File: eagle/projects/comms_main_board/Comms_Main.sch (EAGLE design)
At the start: 96 parts, among them J1 RECE-20279-001E, J2 PRT-12639, J3 PRT-12639, J4 PRT-12639, J5 PRT-12639, J6 MOL-KK-3P-RA, J7 MOL-KK-5P-V, J8 RECEPTACLE-2x20-254MM, Q1 CSD17579Q3A, U1 TPS562209DDCT, U11 TPS562209DDCT, U2 LP2985-33DBVR, U3 LP5900TLX-3.3/NOPB, U4 TPS562209DDCT, U5 LMZ34002RKGR, U6 LM3488MMX/NOPB, U7 PCT2075D,118, U8 MS560702BA03-50, U9 MAX-M8Q

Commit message: PTT Switch, ATV POT Connector
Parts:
- added J9: MOL-KK-3P-RA, daqcs:MOLKK_3PIN_3RA_RA
- added R36: 0.0, comms:RES_0R0_0805
- added R37: 1k, comms:RES_1R0_0603
- added U12: (no value), comms:MMBT3904-7-F
- J1: value RECE-20279-001E -> (none); device comms:IPEX-20279-001E -> comms:SMA_EDGE
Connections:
- new net N$52: R36.1, U12.E
- new net N$53: R37.2, U12.B
- new net POT_A: J9.1
- new net POT_B: J9.2
- new net POT_W: J9.3
- new net PTT_GPIO: R37.1
- net GND: now also J1.GND@0, J1.GND@2, J1.GND@3, R36.2
- net N$24: now also J1.SIGNAL; no longer J1.1
- net PTT: now also U12.C
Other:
- note added: "ATV POT Connector"
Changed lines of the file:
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@@
 <part name="FRAME4" library="frames" deviceset="A4L-LOC" device=""/>
 <part name="SUPPLY6" library="supply2" deviceset="GND" device=""/>
-<part name="J1" library="comms" deviceset="IPEX-20279-001E" device="" value="RECE-20279-001E"/>
 <part name="R16" library="comms" deviceset="RES" device="_0603" technology="_0R10" value="10"/>
 <part name="C22" library="comms" deviceset="CAP" device="_0805" technology="_10NF0" value="10nF"/>
@@
 <part name="J8" library="comms" deviceset="RECEPTACLE-2X20-254MM" device="" value="RECEPTACLE-2x20-254MM"/>
 <part name="SUPPLY16" library="supply2" deviceset="GND" device=""/>
+<part name="J1" library="comms" deviceset="SMA_EDGE" device=""/>
+<part name="R36" library="comms" deviceset="RES" device="_0805" technology="_0R0" value="0.0"/>
+<part name="SUPPLY17" library="supply2" deviceset="GND" device=""/>
+<part name="U12" library="comms" deviceset="MMBT3904-7-F" device=""/>
+<part name="R37" library="comms" deviceset="RES" device="_0603" technology="_1R0" value="1k"/>
+<part name="J9" library="daqcs" deviceset="MOLKK_3PIN" device="_RA" technology="_3RA" value="MOL-KK-3P-RA"/>
 </parts>
 <sheets>
@@
 <instance part="FRAME4" gate="G$1" x="0" y="0"/>
 <instance part="SUPPLY6" gate="GND" x="109.22" y="68.58"/>
-<instance part="J1" gate="G$1" x="55.88" y="116.84"/>
 <instance part="R16" gate="G$1" x="93.98" y="101.6"/>
 <instance part="C22" gate="G$1" x="76.2" y="78.74"/>
@@
 <instance part="R39" gate="G$1" x="167.64" y="101.6"/>
 <instance part="U9" gate="G$1" x="134.62" y="106.68"/>
+<instance part="J1" gate="1" x="53.34" y="116.84"/>
 </instances>
 <busses>
@@
 <segment>
 <pinref part="SUPPLY6" gate="GND" pin="GND"/>
-<wire x1="109.22" y1="121.92" x2="109.22" y2="114.3" width="0.1524" layer="91"/>
-<wire x1="109.22" y1="114.3" x2="109.22" y2="111.76" width="0.1524" layer="91"/>
+<wire x1="109.22" y1="121.92" x2="109.22" y2="111.76" width="0.1524" layer="91"/>
 <wire x1="109.22" y1="111.76" x2="109.22" y2="76.2" width="0.1524" layer="91"/>
 <wire x1="109.22" y1="76.2" x2="109.22" y2="73.66" width="0.1524" layer="91"/>
@@
 <junction x="109.22" y="73.66"/>
 <wire x1="111.76" y1="121.92" x2="109.22" y2="121.92" width="0.1524" layer="91"/>
-<pinref part="J1" gate="G$1" pin="GND@1"/>
-<wire x1="58.42" y1="114.3" x2="109.22" y2="114.3" width="0.1524" layer="91"/>
-<junction x="109.22" y="114.3"/>
 <pinref part="C22" gate="G$1" pin="2"/>
 <wire x1="76.2" y1="76.2" x2="109.22" y2="76.2" width="0.1524" layer="91"/>
@@
 <pinref part="U9" gate="G$1" pin="10_GND"/>
 <pinref part="U9" gate="G$1" pin="12_GND"/>
+<pinref part="J1" gate="1" pin="GND@0"/>
+<wire x1="50.8" y1="111.76" x2="48.26" y2="111.76" width="0.1524" layer="91"/>
+<wire x1="48.26" y1="111.76" x2="48.26" y2="109.22" width="0.1524" layer="91"/>
+<wire x1="48.26" y1="109.22" x2="48.26" y2="106.68" width="0.1524" layer="91"/>
+<wire x1="48.26" y1="106.68" x2="48.26" y2="104.14" width="0.1524" layer="91"/>
+<wire x1="48.26" y1="104.14" x2="48.26" y2="76.2" width="0.1524" layer="91"/>
+<wire x1="48.26" y1="76.2" x2="76.2" y2="76.2" width="0.1524" layer="91"/>
+<junction x="76.2" y="76.2"/>
+<pinref part="J1" gate="1" pin="GND@1"/>
+<wire x1="50.8" y1="109.22" x2="48.26" y2="109.22" width="0.1524" layer="91"/>
+<junction x="48.26" y="109.22"/>
+<pinref part="J1" gate="1" pin="GND@2"/>
+<wire x1="50.8" y1="106.68" x2="48.26" y2="106.68" width="0.1524" layer="91"/>
+<junction x="48.26" y="106.68"/>
+<pinref part="J1" gate="1" pin="GND@3"/>
+<wire x1="50.8" y1="104.14" x2="48.26" y2="104.14" width="0.1524" layer="91"/>
+<junction x="48.26" y="104.14"/>
 </segment>
 </net>
 <net name="N$24" class="0">
 <segment>
-<pinref part="J1" gate="G$1" pin="1"/>
 <wire x1="58.42" y1="116.84" x2="76.2" y2="116.84" width="0.1524" layer="91"/>
 <pinref part="L5" gate="G$1" pin="1"/>
@@
 <junction x="76.2" y="116.84"/>
 <pinref part="U9" gate="G$1" pin="11_RF_IN"/>
+<pinref part="J1" gate="1" pin="SIGNAL"/>
 </segment>
 </net>
@@
 <instance part="J4" gate="G$1" x="55.88" y="66.04"/>
 <instance part="J5" gate="G$1" x="55.88" y="40.64"/>
+<instance part="R36" gate="G$1" x="180.34" y="76.2" rot="R270"/>
+<instance part="SUPPLY17" gate="GND" x="180.34" y="66.04"/>
+<instance part="U12" gate="A" x="180.34" y="93.98"/>
+<instance part="R37" gate="G$1" x="157.48" y="93.98"/>
 </instances>
 <busses>
@@
 <pinref part="J2" gate="G$1" pin="EARTH"/>
 </segment>
+<segment>
+<pinref part="SUPPLY17" gate="GND" pin="GND"/>
+<pinref part="R36" gate="G$1" pin="2"/>
+<wire x1="180.34" y1="68.58" x2="180.34" y2="71.12" width="0.1524" layer="91"/>
+</segment>
 </net>
 <net name="N$32" class="0">
@@
 <segment>
 <pinref part="R27" gate="G$1" pin="1"/>
-<wire x1="132.08" y1="109.22" x2="167.64" y2="109.22" width="0.1524" layer="91"/>
+<wire x1="132.08" y1="109.22" x2="180.34" y2="109.22" width="0.1524" layer="91"/>
 <label x="154.94" y="109.22" size="1.778" layer="95"/>
+<wire x1="180.34" y1="109.22" x2="180.34" y2="104.14" width="0.1524" layer="91"/>
+<pinref part="U12" gate="A" pin="C"/>
+</segment>
+</net>
+<net name="N$52" class="0">
+<segment>
+<pinref part="R36" gate="G$1" pin="1"/>
+<wire x1="180.34" y1="81.28" x2="180.34" y2="86.36" width="0.1524" layer="91"/>
+<pinref part="U12" gate="A" pin="E"/>
+<wire x1="180.34" y1="81.28" x2="180.34" y2="83.82" width="0.1524" layer="91"/>
+</segment>
+</net>
+<net name="N$53" class="0">
+<segment>
+<pinref part="U12" gate="A" pin="B"/>
+<pinref part="R37" gate="G$1" pin="2"/>
+<wire x1="172.72" y1="93.98" x2="162.56" y2="93.98" width="0.1524" layer="91"/>
+</segment>
+</net>
+<net name="PTT_GPIO" class="0">
+<segment>
+<pinref part="R37" gate="G$1" pin="1"/>
+<wire x1="152.4" y1="93.98" x2="132.08" y2="93.98" width="0.1524" layer="91"/>
+<label x="134.62" y="93.98" size="1.778" layer="95"/>
 </segment>
 </net>
@@
 <text x="-73.66" y="38.1" size="1.778" layer="91">DAQCS SPI Connector</text>
 <text x="66.04" y="-45.72" size="1.778" layer="91">Pi Zero Connector</text>
+<text x="-110.49" y="6.35" size="1.778" layer="91">ATV POT Connector</text>
 </plain>
 <instances>
@@
 <instance part="J8" gate="G$1" x="76.2" y="12.7"/>
 <instance part="SUPPLY16" gate="GND" x="76.2" y="-55.88"/>
+<instance part="J9" gate="G$1" x="-106.68" y="22.86"/>
 </instances>
 <busses>
@@
 </segment>
 </net>
+<net name="POT_A" class="0">
+<segment>
+<pinref part="J9" gate="G$1" pin="1"/>
+<wire x1="-93.98" y1="27.94" x2="-81.28" y2="27.94" width="0.1524" layer="91"/>
+<label x="-91.44" y="27.94" size="1.778" layer="95"/>
+</segment>
+</net>
+<net name="POT_B" class="0">
+<segment>
+<pinref part="J9" gate="G$1" pin="2"/>
+<wire x1="-93.98" y1="22.86" x2="-81.28" y2="22.86" width="0.1524" layer="91"/>
+<label x="-91.44" y="22.86" size="1.778" layer="95"/>
+</segment>
+</net>
+<net name="POT_W" class="0">
+<segment>
+<pinref part="J9" gate="G$1" pin="3"/>
+<wire x1="-93.98" y1="17.78" x2="-81.28" y2="17.78" width="0.1524" layer="91"/>
+<label x="-91.44" y="17.78" size="1.778" layer="95"/>
+</segment>
+</net>

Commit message: Did schematic for RS232 level converter. Started work for analog video mux
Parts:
- added C30, C31, C32, C33, C34: 100nF, comms:CAP_100NF0_0805
- added J10: MOL-KK-2-RA, daqcs:MOLKK_2PIN_2RA_2RA
- added J11, J12, J13, J14: MOL-KK-3P-RA, daqcs:MOLKK_3PIN_3RA_RA
- added U13: (no value), comms:MAX232SOIC16
- added U14: MAX4311, comms:MAX4311EEE
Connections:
- new net N$54: C30.1, U13.C1+
- new net N$55: C30.2, U13.C1-
- new net N$56: C31.1, U13.C2+
- new net N$57: C31.2, U13.C2-
- new net OSD_DATA: U13.T1OUT
- new net UART_TXD: U13.T1IN
- new net VID_IN2: U14.IN2
- new net VID_IN3: U14.IN3
- net 3P3V_RS232: now also C32.1, U13.VCC
- net 5V_BOARD: now also C34.1, U13.V+
- net GND: now also C32.2, C33.2, C34.2, U13.GND
- net NEG_5V_BOARD: now also C33.1, U13.V-
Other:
- note added: "Analog Video Camera Connector #1"
- note added: "Analog Video Camera Connector #2"
- note added: "Analog Video Camera Connector #3"
- note added: "Analog Video Camera Connector #4"
- note added: "OSD Data Connector"
- note added: "RS-232 Level Converter"

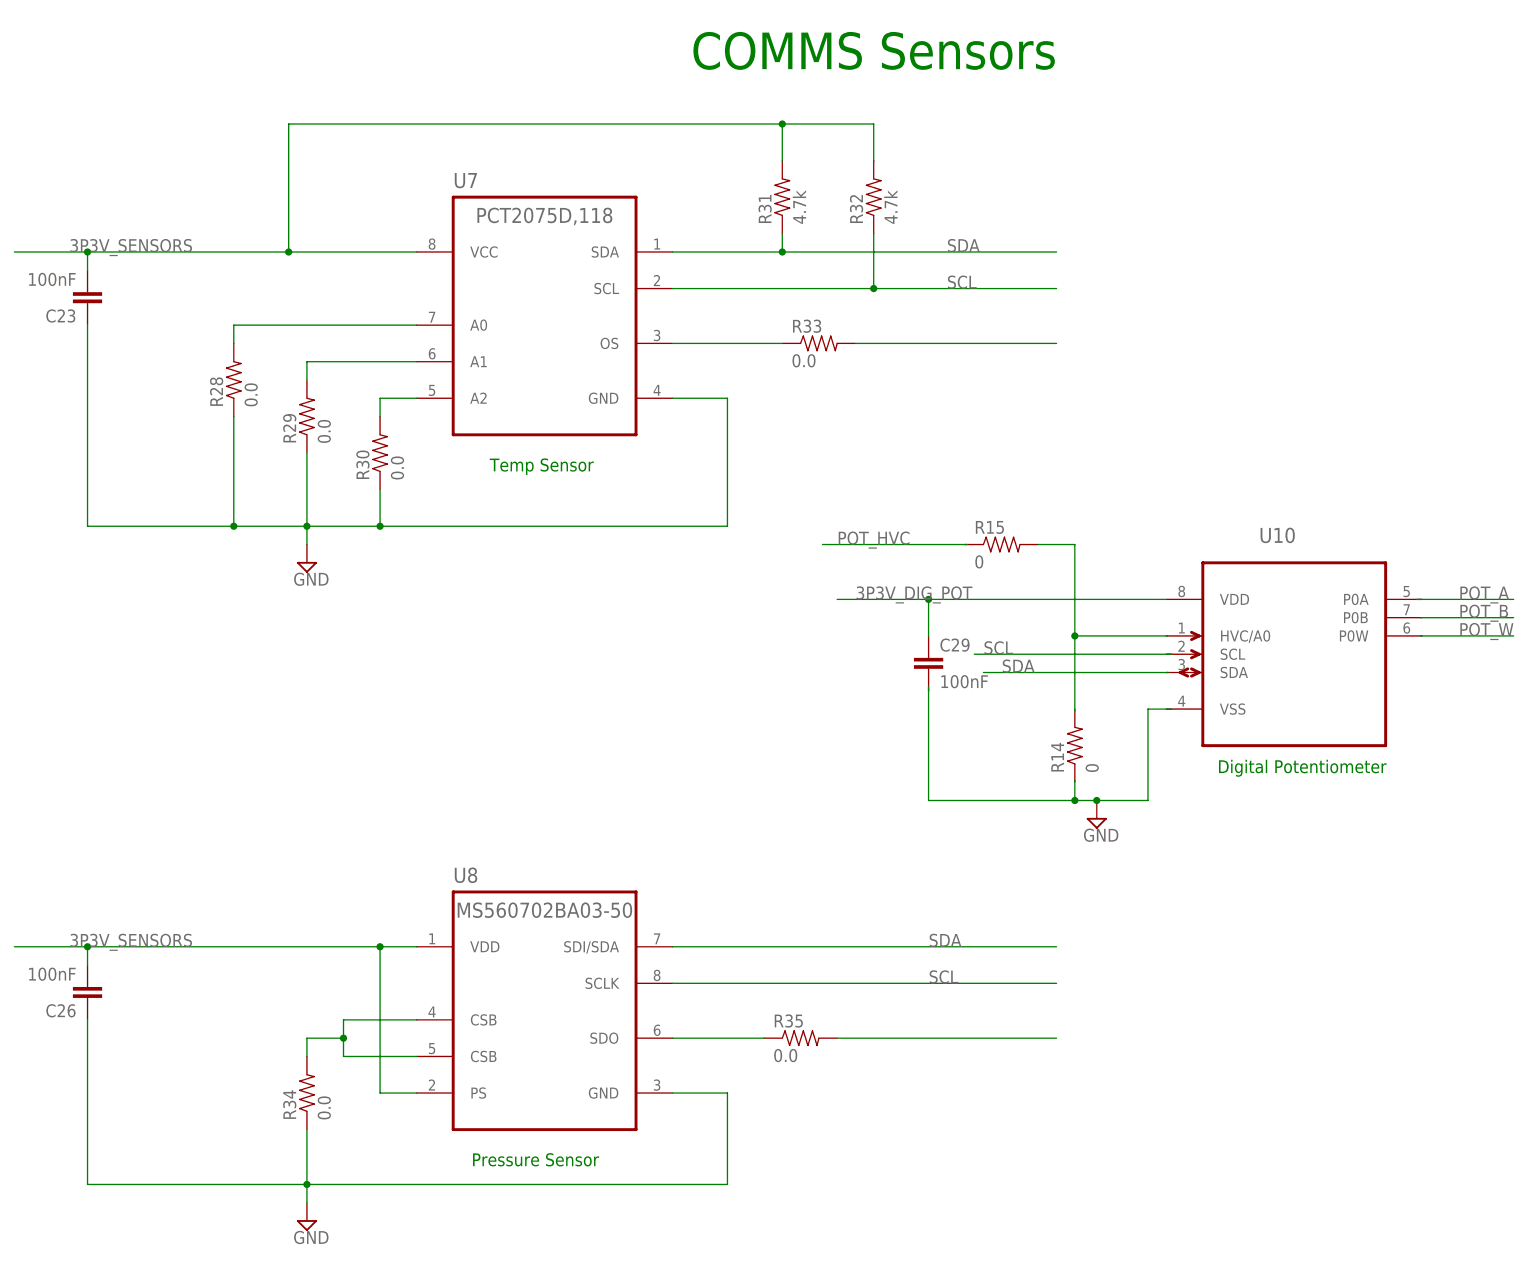
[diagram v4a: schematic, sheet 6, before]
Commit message: Added connectors, video mux details
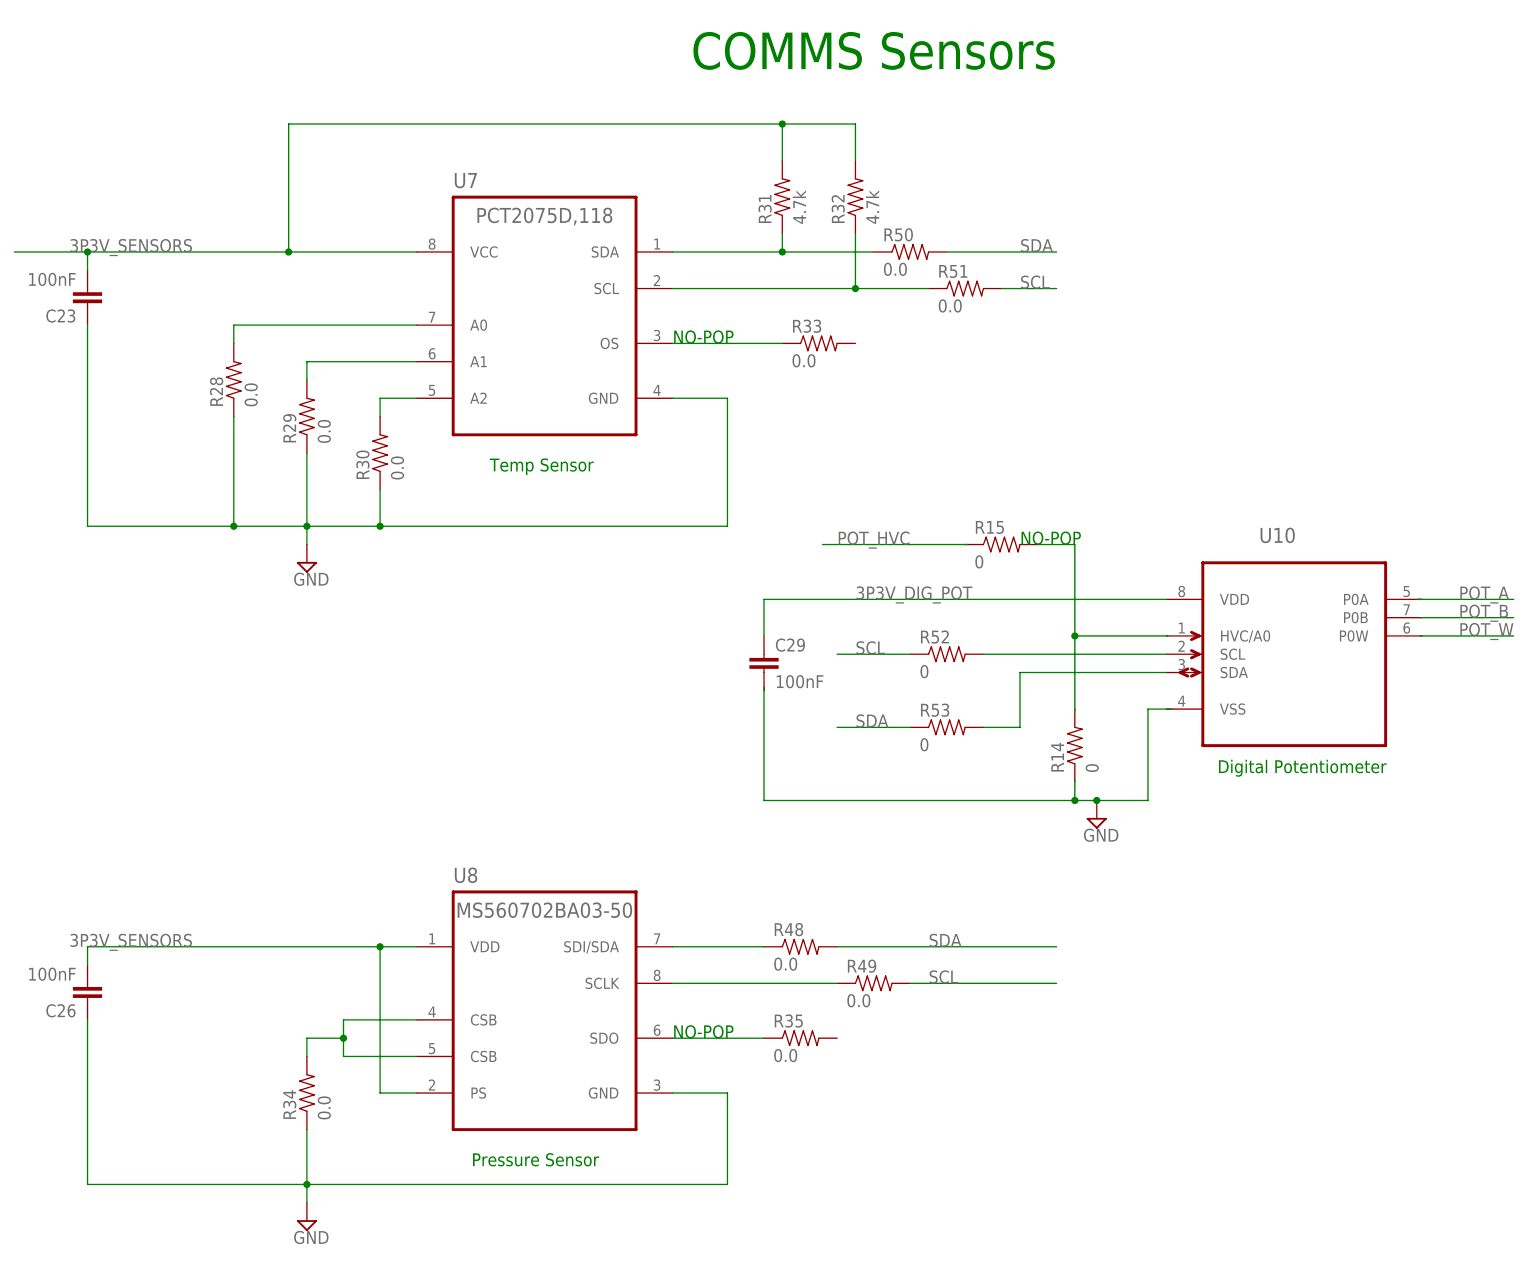
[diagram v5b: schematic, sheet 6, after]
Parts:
- added C35: 100nF, comms:CAP_100NF0_0805
- added J15, J20: MOL-KK-2-RA, daqcs:MOLKK_2PIN_2RA_2RA
- added J16, J17, J18, J19: MOLKK_POW_2_RA, comms:MOLKK_POW_2PIN
- added R42, R43, R44, R45, R54: 75, comms:RES_0R75_0603
- added R46, R47, R52, R53: 0, comms:RES_0R0_0603
- added R48, R49, R50, R51: 0.0, comms:RES_0R0_0805
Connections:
- removed net TEMP_OS: R33.2
- new net N$58: R46.2, R54.2
- new net N$63: R46.1, R47.2, U14.FB
- new net N$64: R53.2, U10.SDA
- new net PRES_SCL: R49.1, U8.SCLK
- new net PRES_SDA: R48.1, U8.SDI/SDA
- new net TEMP_SCL: R32.1, R51.1, U7.SCL
- new net TEMP_SDA: R31.1, R50.1, U7.SDA
- new net VID_IN0: R42.2
- new net VID_IN1: R43.2
- new net VID_OUT: J15.1, R54.1
- net 11P1V_IN: now also J16.1
- net 12V_BOARD: now also J18.1, J20.1
- net 5V_BOARD: now also C35.1, U14.!SHDN, U14.V+
- net 7P4V_IN: now also J17.1, J19.1
- net GND: now also C35.2, J15.2, J16.2, J17.2, J18.2, J19.2, J20.2, R42.1, R43.1, R44.1, R45.1, R47.1, U14.V-
- net N$49: now also R52.2, U10.SCL; no longer R35.2
- net SCL: now also R49.2, R51.2, R52.1; no longer R32.1, U7.SCL, U8.SCLK
- net SDA: now also R48.2, R50.2, R53.1; no longer R31.1, U7.SDA, U8.SDI/SDA
- net VID_IN2: now also R44.2
- net VID_IN3: now also R45.2
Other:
- note added: "11.1V Battery"
- note added: "2m Transceiver Power"
- note added: "7.4V Battery"
- note added: "ATV Transmitter Power"
- note added: "Analog Video Mux"
- note added: "NO-POP"
- note added: "OSD Power Connector"
- note added: "OSD Video Connector"
- moved on the sheet: C29, R32
